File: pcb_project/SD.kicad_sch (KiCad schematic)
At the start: 21 parts, among them J6 MEM2052-00-195-00-A

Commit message: Add most footprints, missing some inductors and 3 buttons
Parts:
- C71: footprint (none) -> Capacitor_SMD:C_0603_1608Metric_Pad1.08x0.95mm_HandSolder
- C72: footprint (none) -> Capacitor_SMD:C_1206_3216Metric_Pad1.33x1.80mm_HandSolder
- R53, R54, R55, R56, R57, R58, R59, R60, R61, R62, R63, R64: footprint (none) -> Resistor_SMD:R_0805_2012Metric_Pad1.20x1.40mm_HandSolder
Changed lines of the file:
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@@
 			)
 		)
-		(property "Footprint" ""
+		(property "Footprint" "Resistor_SMD:R_0805_2012Metric_Pad1.20x1.40mm_HandSolder"
 			(at 143.002 63.5 90)
 			(effects
@@
 			)
 		)
-		(property "Footprint" ""
+		(property "Footprint" "Resistor_SMD:R_0805_2012Metric_Pad1.20x1.40mm_HandSolder"
 			(at 158.242 63.5 90)
 			(effects
@@
 			)
 		)
-		(property "Footprint" ""
+		(property "Footprint" "Resistor_SMD:R_0805_2012Metric_Pad1.20x1.40mm_HandSolder"
 			(at 125.73 83.058 90)
 			(effects
@@
 			)
 		)
-		(property "Footprint" ""
+		(property "Footprint" "Resistor_SMD:R_0805_2012Metric_Pad1.20x1.40mm_HandSolder"
 			(at 125.73 94.488 90)
 			(effects
@@
 			)
 		)
-		(property "Footprint" ""
+		(property "Footprint" "Resistor_SMD:R_0805_2012Metric_Pad1.20x1.40mm_HandSolder"
 			(at 125.73 80.518 90)
 			(effects
@@
 			)
 		)
-		(property "Footprint" ""
+		(property "Footprint" "Resistor_SMD:R_0805_2012Metric_Pad1.20x1.40mm_HandSolder"
 			(at 148.082 63.5 90)
 			(effects
@@
 			)
 		)
-		(property "Footprint" ""
+		(property "Footprint" "Resistor_SMD:R_0805_2012Metric_Pad1.20x1.40mm_HandSolder"
 			(at 163.322 63.5 90)
 			(effects
@@
 			)
 		)
-		(property "Footprint" ""
+		(property "Footprint" "Resistor_SMD:R_0805_2012Metric_Pad1.20x1.40mm_HandSolder"
 			(at 125.73 86.868 90)
 			(effects
@@
 			)
 		)
-		(property "Footprint" ""
+		(property "Footprint" "Resistor_SMD:R_0805_2012Metric_Pad1.20x1.40mm_HandSolder"
 			(at 137.922 63.5 90)
 			(effects
@@
 			)
 		)
-		(property "Footprint" ""
+		(property "Footprint" "Capacitor_SMD:C_0603_1608Metric_Pad1.08x0.95mm_HandSolder"
 			(at 195.2752 63.5 0)
 			(effects
@@
 			)
 		)
-		(property "Footprint" ""
+		(property "Footprint" "Capacitor_SMD:C_1206_3216Metric_Pad1.33x1.80mm_HandSolder"
 			(at 202.8952 63.5 0)
 			(effects
@@
 			)
 		)
-		(property "Footprint" ""
+		(property "Footprint" "Resistor_SMD:R_0805_2012Metric_Pad1.20x1.40mm_HandSolder"
 			(at 125.73 97.028 90)
 			(effects
@@
 			)
 		)
-		(property "Footprint" ""
+		(property "Footprint" "Resistor_SMD:R_0805_2012Metric_Pad1.20x1.40mm_HandSolder"
 			(at 125.73 89.408 90)
 			(effects
@@
 			)
 		)
-		(property "Footprint" ""
+		(property "Footprint" "Resistor_SMD:R_0805_2012Metric_Pad1.20x1.40mm_HandSolder"
 			(at 153.162 63.5 90)
 			(effects

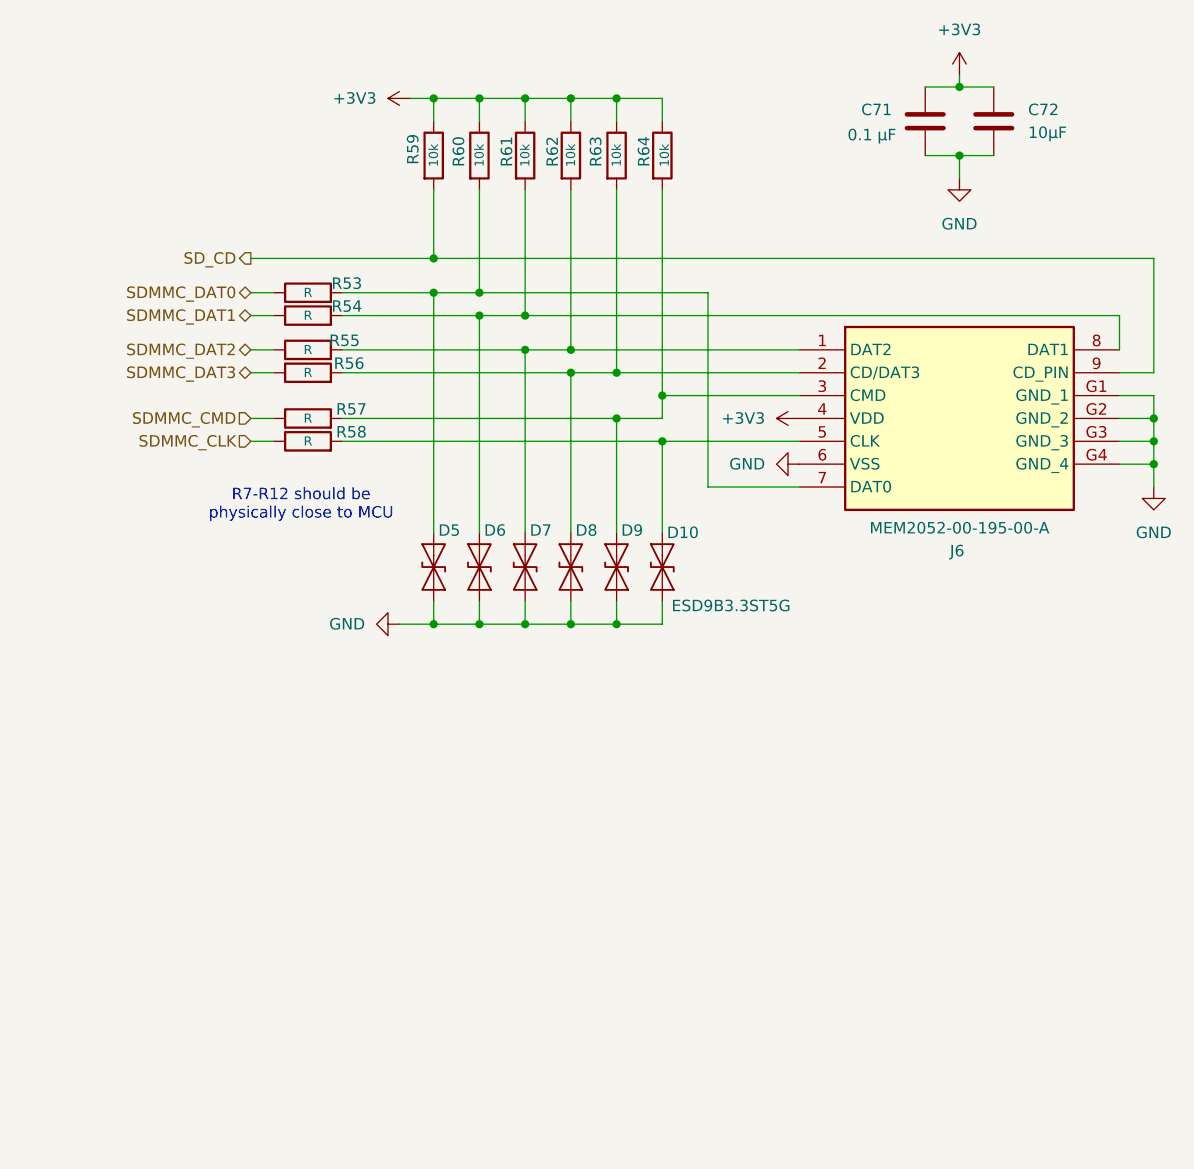
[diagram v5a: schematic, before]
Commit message: Minor schematic changes for easier Layout
- Proper TVS symbol for MicroSD
- Rename USB data lines net name to allow for differential routing
- Change SDMMC_CD GPIO to easier MCU pin
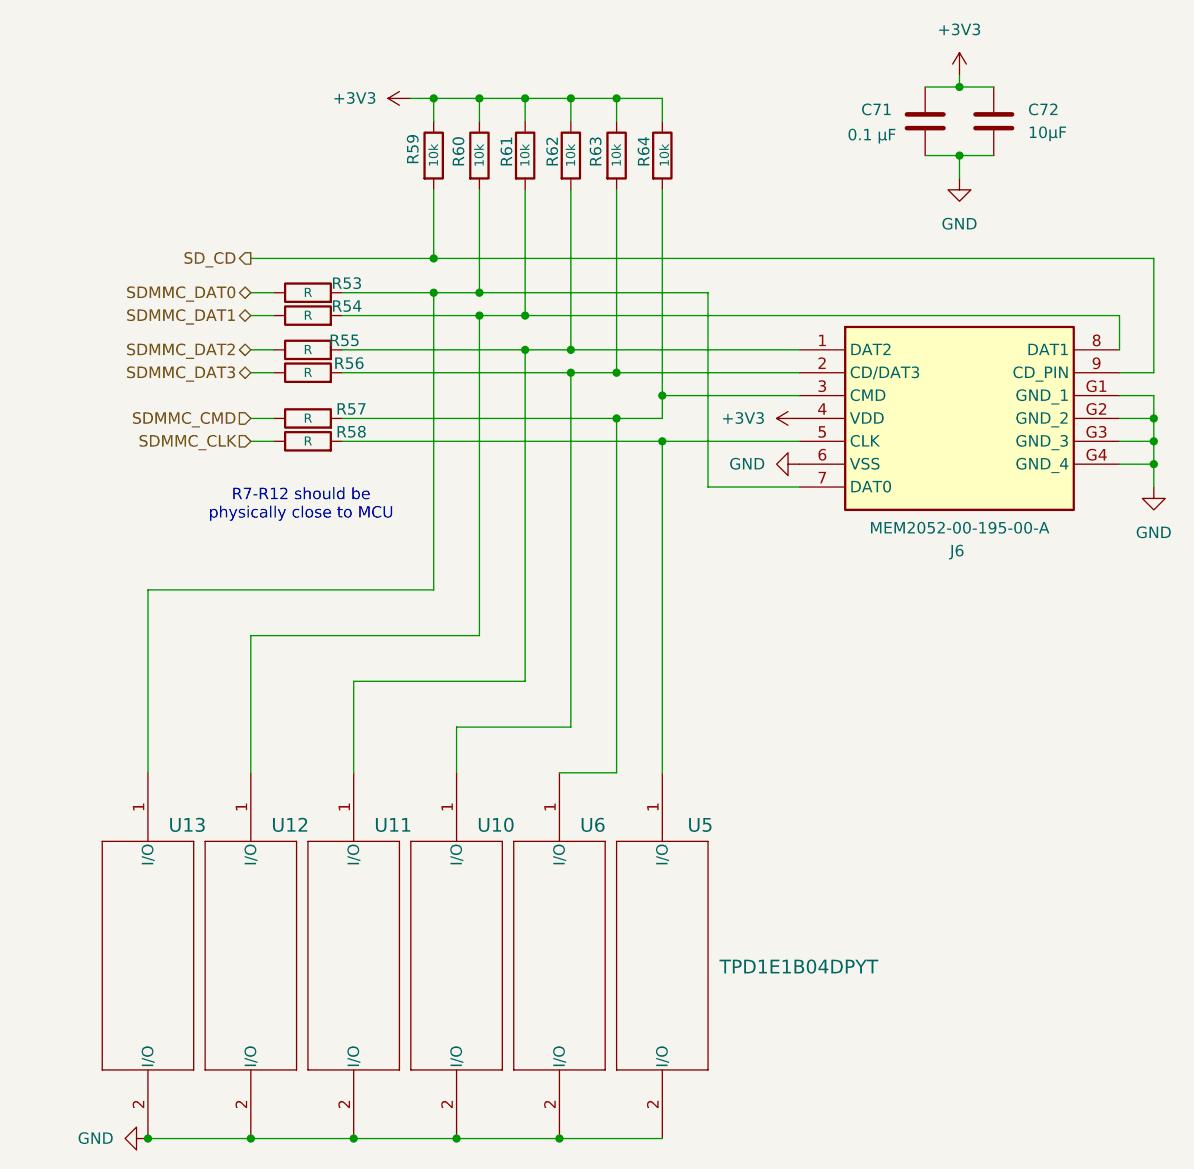
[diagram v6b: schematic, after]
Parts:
- removed D10, D5, D6, D7, D8, D9: ESD9B3.3ST5G, Diode_SMD:D_SOD-923, symbol Diode:ESD9B3.3ST5G
- added U10, U11, U12, U13, U5, U6: TPD1E1B04DPYT, DPY2_TEX, symbol 2025-09-27_10-20-59:TPD1E1B04DPYT
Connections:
- net GND: now also U10.2 (I/O), U11.2 (I/O), U12.2 (I/O), U13.2 (I/O), U5.2 (I/O), U6.2 (I/O)
- net at J6.7 (DAT0), R53.2, R60.2: now also U13.1 (I/O)
- net at J6.2 (CD/DAT3), R56.2, R63.2: now also U10.1 (I/O)
- net at J6.1 (DAT2), R55.2, R62.2: now also U11.1 (I/O)
- net at J6.3 (CMD), R57.2, R64.2: now also U6.1 (I/O)
- net at J6.8 (DAT1), R54.2, R61.2: now also U12.1 (I/O)
- net at J6.5 (CLK), R58.2: now also U5.1 (I/O)

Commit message: Update controller connector schematic
- Fix pin component so it works in layout
- Move RC filters from controller to PCB
- Remove pullups from controller as they are on pcb
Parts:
- U10, U11, U12, U13, U5, U6: footprint DPY2_TEX -> Project_Footprints:DPY2_TEX
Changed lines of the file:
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@@
 			)
 		)
-		(property "Footprint" "DPY2_TEX"
+		(property "Footprint" "Project_Footprints:DPY2_TEX"
 			(at 119.38 132.08 0)
 			(effects
@@
 			)
 		)
-		(property "Footprint" "DPY2_TEX"
+		(property "Footprint" "Project_Footprints:DPY2_TEX"
 			(at 107.95 132.08 0)
 			(effects
@@
 			)
 		)
-		(property "Footprint" "DPY2_TEX"
+		(property "Footprint" "Project_Footprints:DPY2_TEX"
 			(at 142.24 132.08 0)
 			(effects
@@
 			)
 		)
-		(property "Footprint" "DPY2_TEX"
+		(property "Footprint" "Project_Footprints:DPY2_TEX"
 			(at 130.81 132.08 0)
 			(effects
@@
 			)
 		)
-		(property "Footprint" "DPY2_TEX"
+		(property "Footprint" "Project_Footprints:DPY2_TEX"
 			(at 153.67 132.08 0)
 			(effects
@@
 			)
 		)
-		(property "Footprint" "DPY2_TEX"
+		(property "Footprint" "Project_Footprints:DPY2_TEX"
 			(at 165.1 132.08 0)
 			(effects
